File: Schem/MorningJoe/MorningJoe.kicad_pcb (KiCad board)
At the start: 4 copper layers, 160 x 64.4 mm, 58 parts, among them J1 DE15_Socket_HighDensity_Mount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, J5 pBITzBus, SW1 SW_Coded_SH-7070, U1 CD74HC139M96, U10 MK4164N, U11 74HC688, U12 MK4164N, U13 MK4164N, U14 MK4164N, U15 MK4164N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

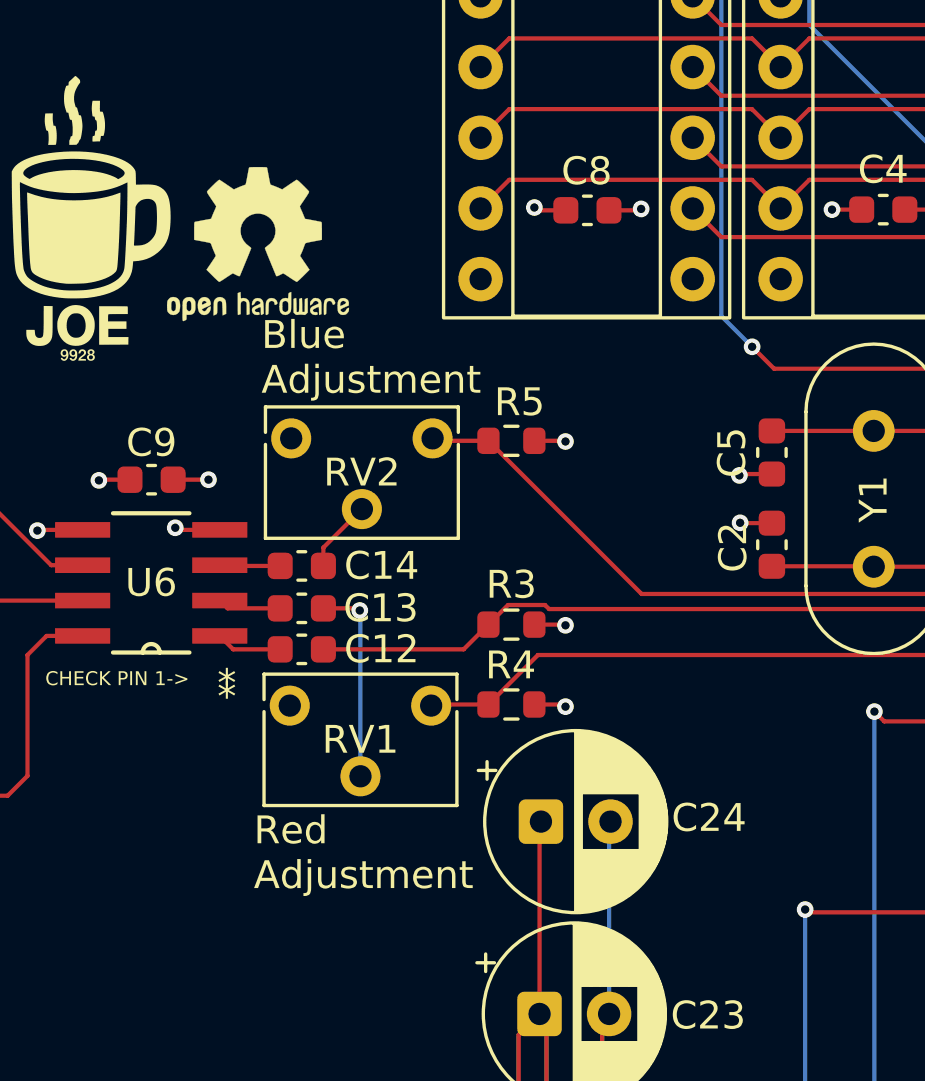
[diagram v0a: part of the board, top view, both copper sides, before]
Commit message: Added bulk caps and fixed up the part numbers
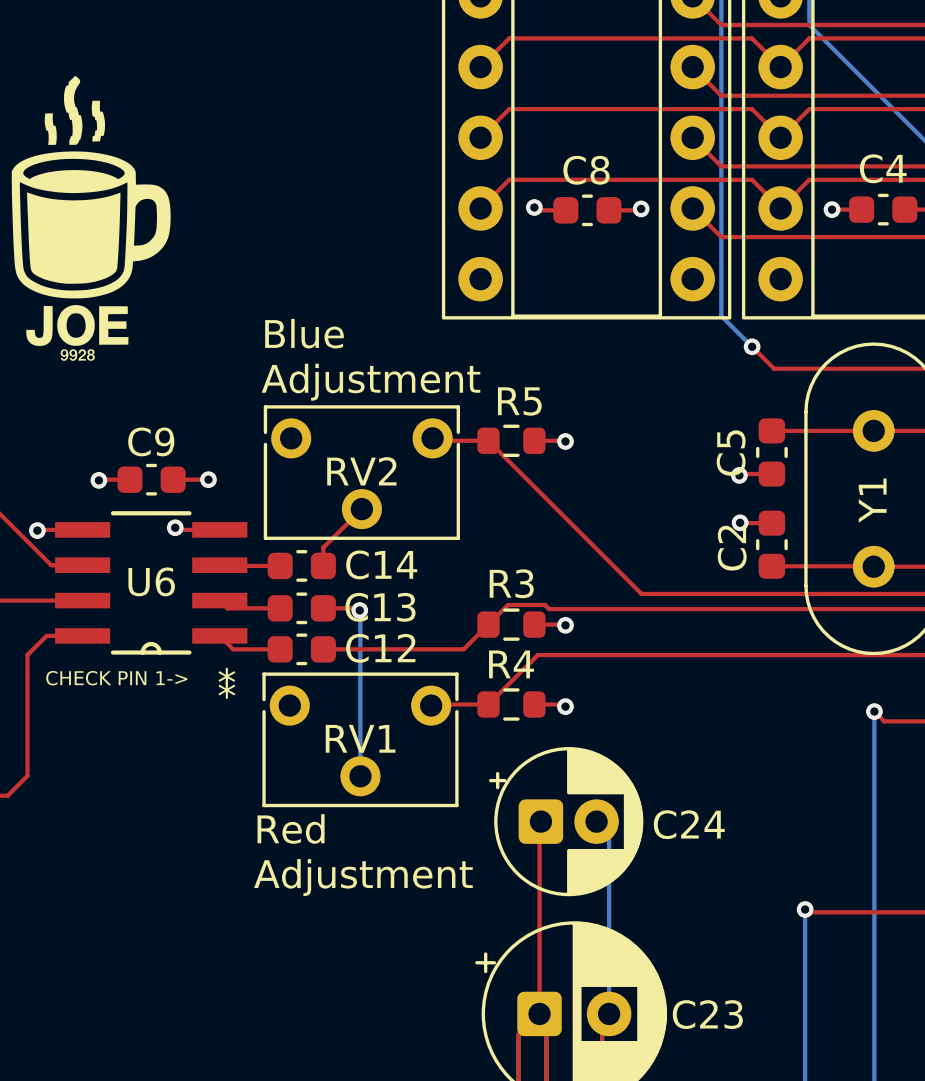
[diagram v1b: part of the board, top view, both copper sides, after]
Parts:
- removed REF**: OSHW-Logo2_7.3x6mm_SilkScreen, Symbol:OSHW-Logo2_7.3x6mm_SilkScreen
- C24: footprint Capacitor_THT:CP_Radial_D6.3mm_P2.50mm -> Capacitor_THT:CP_Radial_D5.0mm_P2.00mm

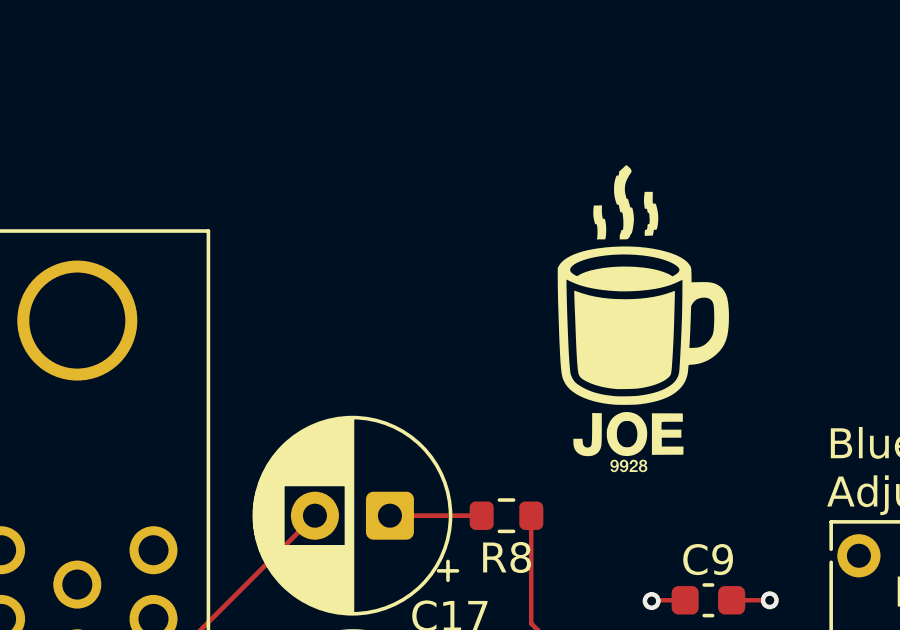
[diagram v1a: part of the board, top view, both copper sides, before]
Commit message: For some reason the OpenSource Hardware Logo had disapeared
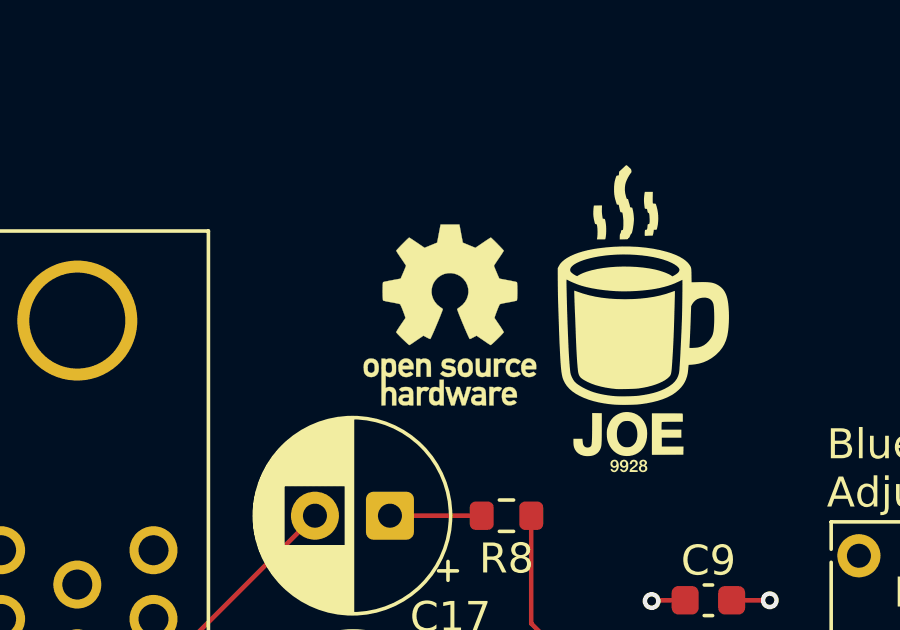
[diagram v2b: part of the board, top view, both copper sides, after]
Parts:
- added REF**: OSHW-Logo_5.7x6mm_SilkScreen, Symbol:OSHW-Logo_5.7x6mm_SilkScreen, F.Cu at (106.2, 72.8)

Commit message: Production Information
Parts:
- added G***: LOGO, Footprints:pBITzlogo-Silk, F.Cu at (235.9, 94.5)
